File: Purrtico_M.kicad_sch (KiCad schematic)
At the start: 53 parts, among them J2 Conn_01x02, J3 Conn_01x03, J4 Conn_01x02, U1 OPA1679, U2 OPA1679

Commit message: update pcb
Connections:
- net GND: now also U1.10 (+); no longer U1.12 (+)
- net at C4.1, R19.2, R2.1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: now also U2.13 (-); no longer U2.9 (-)
- net at C2.1, C4.2, C6.1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: now also U2.14; no longer U2.8
- net at C3.1, R1.1, R3.2: now also U1.9 (-); no longer U1.13 (-)
- net at C1.1, C3.2, R1.2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: now also U1.8; no longer U1.14
- net at R24.1: now also U2.9 (-); no longer U2.13 (-)
- net at R24.2: now also U2.8; no longer U2.14
- net at R23.1: now also U1.13 (-); no longer U1.9 (-)
- net at R23.2: now also U1.14; no longer U1.8
- net at R14.2, R5.2: now also U2.12 (+); no longer U2.10 (+)
- net at R22.2: now also U2.10 (+); no longer U2.12 (+)
- net at R21.2: now also U1.12 (+); no longer U1.10 (+)
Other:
- note added: "1"
- note added: "2"
- note added: "3"
- note added: "4"
- note added: "5"
- note added: "6"
- moved on the sheet: U1C, U1D, U2C, U2D
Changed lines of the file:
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@@
 	)
 	(junction
-		(at 114.3 135.89)
+		(at 161.29 71.12)
 		(diameter 0)
 		(color 0 0 0 0)
 	)
 	(junction
-		(at 116.84 177.8)
+		(at 114.3 135.89)
 		(diameter 0)
 		(color 0 0 0 0)
 	)
 	(junction
-		(at 161.29 71.12)
+		(at 116.84 177.8)
 		(diameter 0)
 		(color 0 0 0 0)
@@
 		)
 	)
+	(text "5"
+		(exclude_from_sim no)
+		(at 185.42 172.466 0)
+		(effects
+			(font
+				(size 1.27 1.27)
+				(bold yes)
+			)
+		)
+	)
+	(text "2"
+		(exclude_from_sim no)
+		(at 153.416 85.344 0)
+		(effects
+			(font
+				(size 1.27 1.27)
+				(bold yes)
+			)
+		)
+	)
 	(text "POLARITY?!"
 		(exclude_from_sim no)
@@
 		)
 	)
+	(text "1"
+		(exclude_from_sim no)
+		(at 67.31 83.058 0)
+		(effects
+			(font
+				(size 1.27 1.27)
+				(thickness 0.254)
+				(bold yes)
+			)
+		)
+	)
 	(text "POLARITY?!"
 		(exclude_from_sim no)
@@
 		)
 	)
+	(text "3"
+		(exclude_from_sim no)
+		(at 104.902 158.496 0)
+		(effects
+			(font
+				(size 1.27 1.27)
+				(bold yes)
+			)
+		)
+	)
+	(text "6"
+		(exclude_from_sim no)
+		(at 127.762 224.282 0)
+		(effects
+			(font
+				(size 1.27 1.27)
+				(bold yes)
+			)
+		)
+	)
+	(text "4"
+		(exclude_from_sim no)
+		(at 150.368 166.624 0)
+		(effects
+			(font
+				(size 1.27 1.27)
+				(bold yes)
+			)
+		)
+	)
 	(text "POLARITY?!"
 		(exclude_from_sim no)
@@
 	(symbol
 		(lib_id "Amplifier_Operational:OPA1679")
-		(at 153.67 71.12 0)
-		(mirror x)
+		(at 384.81 204.47 0)
 		(unit 3)
 		(exclude_from_sim no)
@@
 		(dnp no)
 		(property "Reference" "U2"
-			(at 153.67 81.28 0)
+			(at 384.81 194.31 0)
 			(effects
 				(font
@@
 		)
 		(property "Value" "OPA1679"
-			(at 153.67 78.74 0)
+			(at 384.81 196.85 0)
 			(effects
 				(font
@@
 		)
 		(property "Footprint" "Package_SO:SOIC-14_3.9x8.7mm_P1.27mm"
-			(at 152.4 73.66 0)
+			(at 383.54 201.93 0)
 			(effects
 				(font
@@
 		)
 		(property "Datasheet" "http://www.ti.com/lit/ds/symlink/opa1678.pdf"
-			(at 154.94 76.2 0)
+			(at 386.08 199.39 0)
 			(effects
 				(font
@@
 		)
 		(property "Description" "Low-Distortion Audio Operational Amplifiers, SOIC-14/TSSOP-14"
-			(at 153.67 71.12 0)
+			(at 384.81 204.47 0)
 			(effects
 				(font
@@
 	(symbol
 		(lib_id "Amplifier_Operational:OPA1679")
-		(at 69.85 68.58 0)
-		(mirror x)
+		(at 383.54 177.8 0)
 		(unit 4)
 		(exclude_from_sim no)
@@
 		(dnp no)
 		(property "Reference" "U1"
-			(at 69.85 78.74 0)
+			(at 383.54 167.64 0)
 			(effects
 				(font
@@
 		)
 		(property "Value" "OPA1679"
-			(at 69.85 76.2 0)
+			(at 383.54 170.18 0)
 			(effects
 				(font
@@
 		)
 		(property "Footprint" "Package_SO:SOIC-14_3.9x8.7mm_P1.27mm"
-			(at 68.58 71.12 0)
+			(at 382.27 175.26 0)
 			(effects
 				(font
@@
 		)
 		(property "Datasheet" "http://www.ti.com/lit/ds/symlink/opa1678.pdf"
-			(at 71.12 73.66 0)
+			(at 384.81 172.72 0)
 			(effects
 				(font
@@
 		)
 		(property "Description" "Low-Distortion Audio Operational Amplifiers, SOIC-14/TSSOP-14"
-			(at 69.85 68.58 0)
+			(at 383.54 177.8 0)
 			(effects
 				(font
@@
 	(symbol
 		(lib_id "Amplifier_Operational:OPA1679")
-		(at 384.81 204.47 0)
+		(at 153.67 71.12 0)
+		(mirror x)
 		(unit 4)
 		(exclude_from_sim no)
@@
 		(dnp no)
 		(property "Reference" "U2"
-			(at 384.81 194.31 0)
+			(at 153.67 81.28 0)
 			(effects
 				(font
@@
 		)
 		(property "Value" "OPA1679"
-			(at 384.81 196.85 0)
+			(at 153.67 78.74 0)
 			(effects
 				(font
@@
 		)
 		(property "Footprint" "Package_SO:SOIC-14_3.9x8.7mm_P1.27mm"
-			(at 383.54 201.93 0)
+			(at 152.4 73.66 0)
 			(effects
 				(font
@@
 		)
 		(property "Datasheet" "http://www.ti.com/lit/ds/symlink/opa1678.pdf"
-			(at 386.08 199.39 0)
+			(at 154.94 76.2 0)
 			(effects
 				(font
@@
 		)
 		(property "Description" "Low-Distortion Audio Operational Amplifiers, SOIC-14/TSSOP-14"
-			(at 384.81 204.47 0)
+			(at 153.67 71.12 0)
 			(effects
 				(font
@@
 	(symbol
 		(lib_id "Amplifier_Operational:OPA1679")
-		(at 383.54 177.8 0)
+		(at 69.85 68.58 0)
+		(mirror x)
 		(unit 3)
 		(exclude_from_sim no)
@@
 		(dnp no)
 		(property "Reference" "U1"
-			(at 383.54 167.64 0)
+			(at 69.85 78.74 0)
 			(effects
 				(font
@@
 		)
 		(property "Value" "OPA1679"
-			(at 383.54 170.18 0)
+			(at 69.85 76.2 0)
 			(effects
 				(font
@@
 		)
 		(property "Footprint" "Package_SO:SOIC-14_3.9x8.7mm_P1.27mm"
-			(at 382.27 175.26 0)
+			(at 68.58 71.12 0)
 			(effects
 				(font
@@
 		)
 		(property "Datasheet" "http://www.ti.com/lit/ds/symlink/opa1678.pdf"
-			(at 384.81 172.72 0)
+			(at 71.12 73.66 0)
 			(effects
 				(font
@@
 		)
 		(property "Description" "Low-Distortion Audio Operational Amplifiers, SOIC-14/TSSOP-14"
-			(at 383.54 177.8 0)
+			(at 69.85 68.58 0)
 			(effects
 				(font

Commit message: update pcb
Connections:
- net at C8.2, R11.1, R18.2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: now also U1.7; no longer U1.1
- net at C8.1, R10.2: now also U1.6 (-); no longer U1.2 (-)
- net at C9.1, R13.1: now also U1.2 (-); no longer U1.6 (-)
- net at C9.2, R6.2: now also U1.1; no longer U1.7
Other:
- moved on the sheet: U1A, U1B
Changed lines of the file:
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@@
 	)
 	(junction
-		(at 254 264.16)
+		(at 184.15 157.48)
 		(diameter 0)
 		(color 0 0 0 0)
 	)
 	(junction
-		(at 140.97 198.12)
+		(at 254 264.16)
 		(diameter 0)
 		(color 0 0 0 0)
 	)
 	(junction
-		(at 184.15 157.48)
+		(at 140.97 198.12)
 		(diameter 0)
 		(color 0 0 0 0)
@@
 	(wire
 		(pts
-			(xy 184.15 149.86) (xy 184.15 157.48)
-		)
-		(stroke
-			(width 0)
-			(type default)
-		)
-	)
-	(wire
-		(pts
 			(xy 391.16 210.82) (xy 392.43 210.82)
 		)
@@
 	(wire
 		(pts
+			(xy 184.15 149.86) (xy 184.15 157.48)
+		)
+		(stroke
+			(width 0)
+			(type default)
+		)
+	)
+	(wire
+		(pts
 			(xy 196.85 73.66) (xy 196.85 76.2)
 		)
@@
 	(symbol
 		(lib_id "Amplifier_Operational:OPA1679")
-		(at 151.13 152.4 0)
+		(at 191.77 160.02 0)
 		(mirror x)
 		(unit 1)
@@
 		(dnp no)
 		(property "Reference" "U1"
-			(at 151.13 162.56 0)
+			(at 191.77 170.18 0)
 			(effects
 				(font
@@
 		)
 		(property "Value" "OPA1679"
-			(at 151.13 160.02 0)
+			(at 191.77 167.64 0)
 			(effects
 				(font
@@
 		)
 		(property "Footprint" "Package_SO:SOIC-14_3.9x8.7mm_P1.27mm"
-			(at 149.86 154.94 0)
+			(at 190.5 162.56 0)
 			(effects
 				(font
@@
 		)
 		(property "Datasheet" "http://www.ti.com/lit/ds/symlink/opa1678.pdf"
-			(at 152.4 157.48 0)
+			(at 193.04 165.1 0)
 			(effects
 				(font
@@
 		)
 		(property "Description" "Low-Distortion Audio Operational Amplifiers, SOIC-14/TSSOP-14"
-			(at 151.13 152.4 0)
+			(at 191.77 160.02 0)
 			(effects
 				(font
@@
 	(symbol
 		(lib_id "Amplifier_Operational:OPA1679")
-		(at 191.77 160.02 0)
+		(at 151.13 152.4 0)
 		(mirror x)
 		(unit 2)
@@
 		(dnp no)
 		(property "Reference" "U1"
-			(at 191.77 170.18 0)
+			(at 151.13 162.56 0)
 			(effects
 				(font
@@
 		)
 		(property "Value" "OPA1679"
-			(at 191.77 167.64 0)
+			(at 151.13 160.02 0)
 			(effects
 				(font
@@
 		)
 		(property "Footprint" "Package_SO:SOIC-14_3.9x8.7mm_P1.27mm"
-			(at 190.5 162.56 0)
+			(at 149.86 154.94 0)
 			(effects
 				(font
@@
 		)
 		(property "Datasheet" "http://www.ti.com/lit/ds/symlink/opa1678.pdf"
-			(at 193.04 165.1 0)
+			(at 152.4 157.48 0)
 			(effects
 				(font
@@
 		)
 		(property "Description" "Low-Distortion Audio Operational Amplifiers, SOIC-14/TSSOP-14"
-			(at 191.77 160.02 0)
+			(at 151.13 152.4 0)
 			(effects
 				(font

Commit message: update routing
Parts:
- removed J3: Conn_01x03, Connector_PinHeader_2.54mm:PinHeader_1x03_P2.54mm_Vertical, symbol Connector_Generic:Conn_01x03
- added J1: Conn_02x05_Odd_Even, Connector_PinHeader_2.54mm:PinHeader_2x05_P2.54mm_Vertical, symbol Connector_Generic:Conn_02x05_Odd_Even
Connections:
- net +15V: now also C16.2, C17.2, J1.10 (Pin_10), J1.9 (Pin_9); no longer C13.1, C14.1
- net -15V: now also C13.1, C14.1, J1.1 (Pin_1), J1.2 (Pin_2); no longer C16.2, C17.2
- net GND: now also U1.12 (+), U2.12 (+), J1.3 (Pin_3), J1.4 (Pin_4), J1.5 (Pin_5), J1.6 (Pin_6), J1.7 (Pin_7), J1.8 (Pin_8); no longer U1.3 (+), U2.5 (+)
- net at C4.1, R19.2, R2.1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: now also U1.2 (-); no longer U2.13 (-)
- net at C2.1, C4.2, C6.1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: now also U1.1; no longer U2.14
- net at C9.2, R6.2: now also U2.1; no longer U1.1
- net at C9.1, R13.1: now also U2.2 (-); no longer U1.2 (-)
- net at C3.1, R1.1, R3.2: now also U1.6 (-); no longer U1.9 (-)
- net at C1.1, C3.2, R1.2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: now also U1.7; no longer U1.8
- net at R23.1: now also U2.6 (-); no longer U1.13 (-)
- net at R23.2: now also U2.7; no longer U1.14
- net at C7.1, R20.1, R6.1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: now also U1.9 (-); no longer U2.2 (-)
- net at C7.2, R7.2, R9.2: now also U1.8; no longer U2.1
- net at R14.2, R5.2: now also U1.3 (+); no longer U2.12 (+)
- net at C11.1, R14.1, R16.1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: now also U1.14; no longer U2.7
- net at R21.2: now also U2.5 (+); no longer U1.12 (+)
- net at C8.1, R10.2: now also U2.13 (-); no longer U1.6 (-)
- net at C8.2, R11.1, R18.2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: now also U2.14; no longer U1.7
- net at C11.2, R17.2, R18.1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: now also U1.13 (-); no longer U2.6 (-)
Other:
- note removed: "1"
- note removed: "2"
- note removed: "3"
- note removed: "4"
- note removed: "5"
- note removed: "6"
- moved on the sheet: C13, C14, C16, C17, U1A, U1B, U1C, U1D, U2A, U2B, U2D

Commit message: added shelving band
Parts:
- removed H3, H4: MountingHole, MountingHole:MountingHole_3.2mm_M3_DIN965_Pad, symbol Mechanical:MountingHole_Pad
- added C18: 22p, Capacitor_SMD:C_1206_3216Metric, symbol Device:C
- added C19: 5n6, Capacitor_THT:C_Rect_L7.2mm_W2.5mm_P5.00mm_FKS2_FKP2_MKS2_MKP2, symbol Device:C
- added C20, C31: 470n, Capacitor_THT:C_Rect_L7.2mm_W2.5mm_P5.00mm_FKS2_FKP2_MKS2_MKP2, symbol Device:C
- added C21: 22u, Capacitor_THT:CP_Radial_D6.3mm_P2.50mm, symbol Device:C_Polarized
- added C22, C25, C26, C29, C30: 100u, Capacitor_THT:CP_Radial_D6.3mm_P2.50mm, symbol Device:C_Polarized
- added C23, C24: 100n, Capacitor_SMD:C_1206_3216Metric, symbol Device:C
- added C27, C28: 100p, Capacitor_SMD:C_1206_3216Metric, symbol Device:C
- added R25: 2k2, Resistor_SMD:R_1206_3216Metric, symbol Device:R
- added R26: 12k, Resistor_SMD:R_1206_3216Metric, symbol Device:R
- added R27, R33: 0R, Resistor_SMD:R_1206_3216Metric, symbol Device:R
- added R28, R30: 100R, Resistor_SMD:R_1206_3216Metric, symbol Device:R
- added R29, R32: 1k5, Resistor_SMD:R_1206_3216Metric, symbol Device:R
- added R31, R34: 390R, Resistor_SMD:R_1206_3216Metric, symbol Device:R
- added R35: 1M, Resistor_SMD:R_1206_3216Metric, symbol Device:R
- added R40, R41, R42, R43: 2k7, Resistor_SMD:R_1206_3216Metric, symbol Device:R
- added R44: 18k, Resistor_SMD:R_1206_3216Metric, symbol Device:R
- added RV4: 10k, Connector_PinHeader_2.54mm:PinHeader_2x03_P2.54mm_Vertical, symbol Device:R_Potentiometer_Dual_Separate
- added RV5: 10k, Connector_PinHeader_2.54mm:PinHeader_1x03_P2.54mm_Vertical, symbol Device:R_Potentiometer
- added RV6: 4k7, Connector_PinHeader_2.54mm:PinHeader_1x03_P2.54mm_Vertical, symbol Device:R_Potentiometer
- added SW1: SW_DPDT_x2, Connector_PinHeader_2.54mm:PinHeader_2x03_P2.54mm_Vertical, symbol Switch:SW_DPDT_x2
- added U3: OPA1679, Package_SO:SOIC-14_3.9x8.7mm_P1.27mm, symbol Amplifier_Operational:OPA1679
- R21, R22: value 0R -> 3M3
- R23: value 0R -> 2k2
- R24: value 0R -> 560R
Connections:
- net +15V: now also C23.2, U3.4 (V+)
- net -15V: now also C24.1, U3.11 (V-)
- net GND: now also U2.5 (+), C23.1, C24.2, R27.1, R31.1, R34.1, RV5.1, RV5.2, U3.10 (+), U3.5 (+); no longer R22.1
- net at U2.9 (-): now also C28.1, R41.1, R43.2; no longer R24.1
- net at R24.2: now also SW1.6 (C); no longer U2.8
- net at U2.6 (-): now also C27.1, R40.1, R42.2; no longer R23.1
- net at R23.2: now also R22.2; no longer U2.7
- net at U2.10 (+): now also C19.2, R30.1, R44.2, U3.7; no longer R22.2
- net at J2.2 (Pin_2): now also C29.1; no longer C5.1
- net at R21.2: now also R22.1, C22.1, SW1.5 (B); no longer U2.5 (+)
- new net: C26.1, RV6.2
- new net: C22.2, C26.2, R44.1, U3.3 (+)
- new net: C18.1, R25.1, R26.1, U3.2 (-)
- new net: C20.2, C21.2, C31.2, R25.2, R35.2, SW1.2 (B)
- new net: C19.1, R29.2, U3.6 (-)
- new net: R27.2, U3.12 (+)
- new net: C25.2, R43.1, RV6.1
- new net: R24.1, RV5.3
- new net: C20.1, C31.1, R32.1, R35.1, SW1.1 (A), U3.9 (-)
- new net: C28.2, C30.1, R41.2, RV6.3, U2.8
- new net: C29.2, R42.1
- new net: C18.2, R26.2, R28.2, U3.1
- new net: C25.1, C27.2, R40.2, U2.7
- new net: R28.1, RV4.1
- new net: R30.2, RV4.4
- new net: R32.2, RV4.5
- new net: R34.2, RV4.6
- new net: R23.1, SW1.4 (A)
- new net: C21.1, U3.8
- new net: R31.2, RV4.3
- new net: R33.1, U3.13 (-)
- new net: R33.2, U3.14
- new net: C30.2, C5.1
- new net: R29.1, RV4.2
- no-connect marks 0 -> 1
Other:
- moved on the sheet: C1, C10, C11, C12, C13, C14, C15, C16, C17, C2, C3, C4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

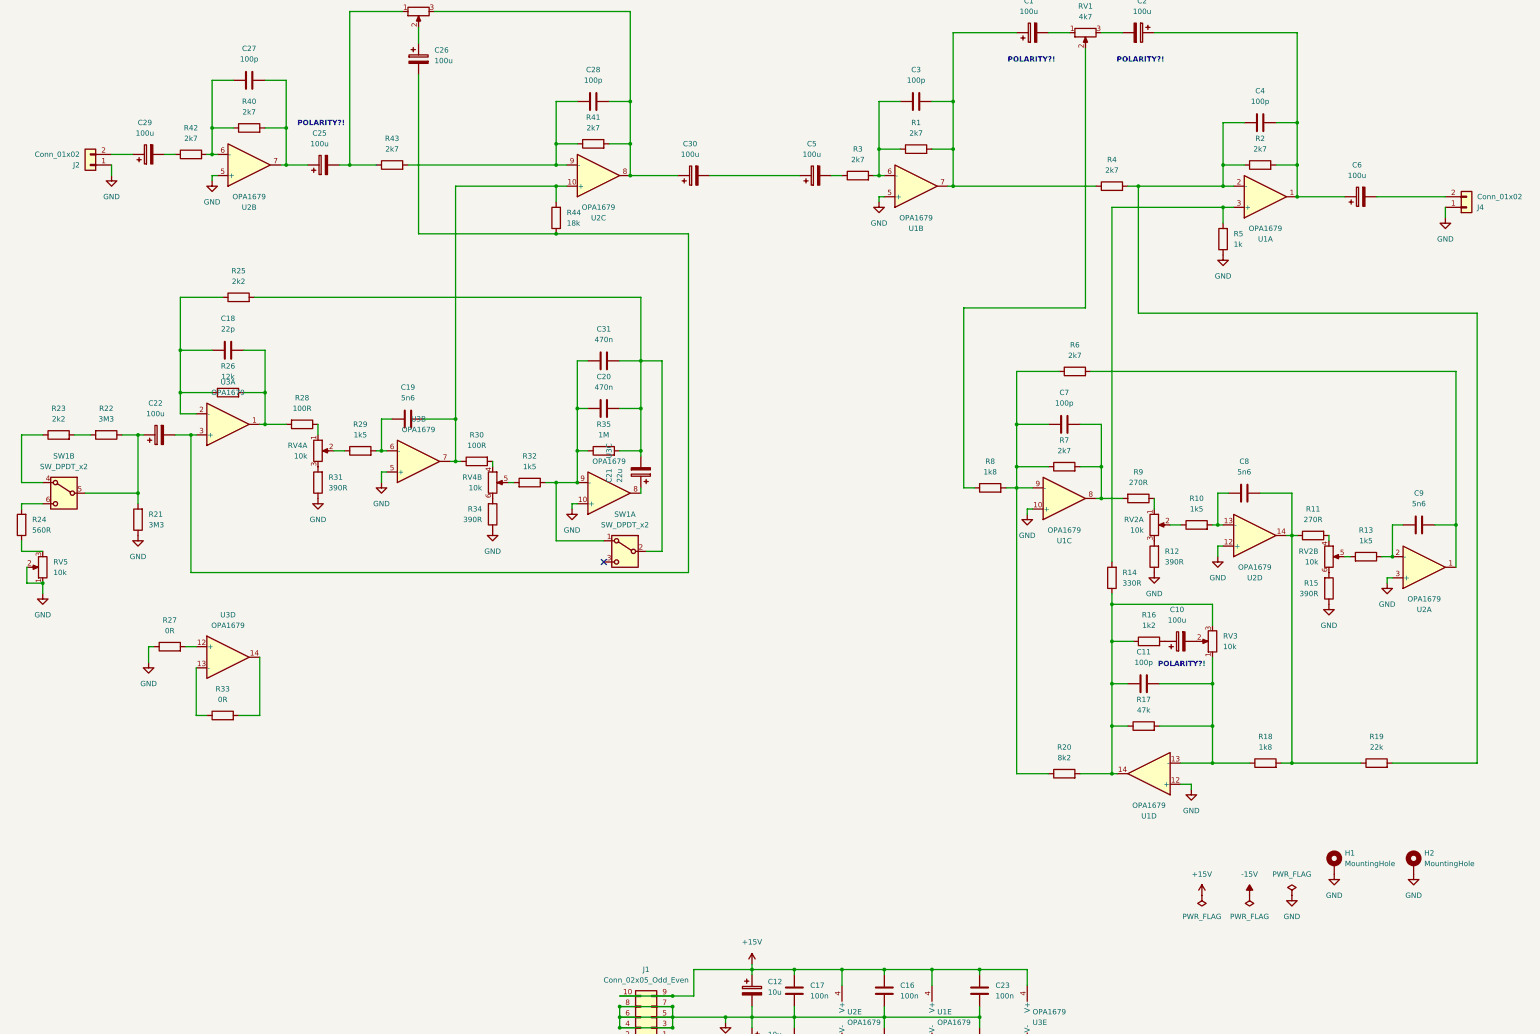
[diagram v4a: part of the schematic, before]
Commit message: modified shelving filter
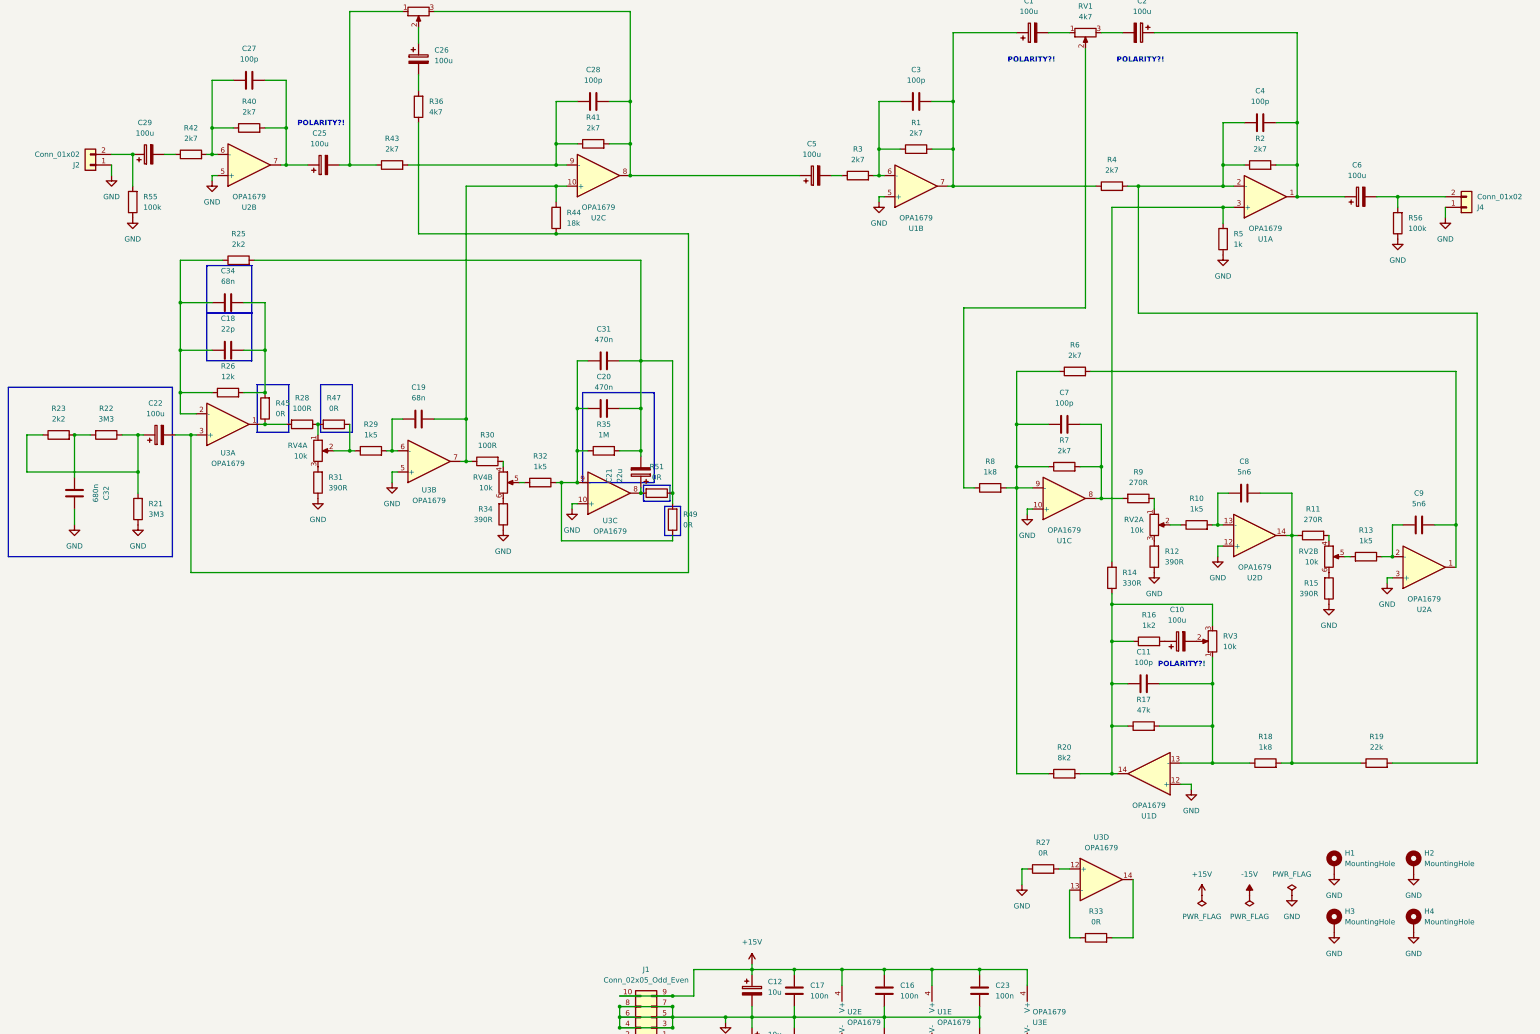
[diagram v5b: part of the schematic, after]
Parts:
- removed C30: 100u, Capacitor_THT:CP_Radial_D6.3mm_P2.50mm, symbol Device:C_Polarized
- removed R24: 560R, Resistor_SMD:R_1206_3216Metric, symbol Device:R
- removed RV5: 10k, Connector_PinHeader_2.54mm:PinHeader_1x03_P2.54mm_Vertical, symbol Device:R_Potentiometer
- removed SW1: SW_DPDT_x2, Connector_PinHeader_2.54mm:PinHeader_2x03_P2.54mm_Vertical, symbol Switch:SW_DPDT_x2
- added C32: 680n, Capacitor_THT:C_Rect_L7.2mm_W2.5mm_P5.00mm_FKS2_FKP2_MKS2_MKP2, symbol Device:C
- added C34: 68n, Capacitor_THT:C_Rect_L7.2mm_W2.5mm_P5.00mm_FKS2_FKP2_MKS2_MKP2, symbol Device:C
- added H3, H4: MountingHole, MountingHole:MountingHole_3.2mm_M3_DIN965_Pad, symbol Mechanical:MountingHole_Pad
- added R36: 4k7, Resistor_SMD:R_1206_3216Metric, symbol Device:R
- added R45, R47, R49, R51: 0R, Resistor_SMD:R_1206_3216Metric, symbol Device:R
- added R55, R56: 100k, Resistor_SMD:R_1206_3216Metric, symbol Device:R
- C19: value 5n6 -> 68n
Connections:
- net GND: now also C32.2, H3.1, H4.1, R55.1, R56.1
- net at C22.2, R44.1, U3.3 (+): now also R36.1; no longer C26.2
- net at C18.1, R25.1, R26.1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: now also C34.1
- net at C20.2, C21.2, C31.2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: now also R49.2, R51.1
- net at C20.1, C31.1, R32.1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: now also R49.1
- net at C22.1, R21.2, R22.1: now also R23.1
- net at R22.2, R23.2: now also C32.1
- net at C28.2, R41.2, RV6.3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: now also C5.1
- net at C29.1, J2.2 (Pin_2): now also R55.2
- net at R28.2, U3.1: now also R45.1; no longer C18.2, R26.2
- net at R28.1, RV4.1: now also R47.2
- net at C6.2, J4.2 (Pin_2): now also R56.2
- net at C21.1, U3.8: now also R51.2
- net at R29.1, RV4.2: now also R47.1
- new net: C26.2, R36.2
- new net: C18.2, C34.2, R26.2, R45.2
- no-connect marks 1 -> 0
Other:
- moved on the sheet: C19, R21, R25, R27, R29, R30, R32, R33, R34, RV4B, U3B, U3D
